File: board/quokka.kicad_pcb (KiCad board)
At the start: 4 copper layers, 228.6 x 184.1 mm, 337 parts, among them J1301 FPGA JTAG, J201 Barrel_Jack, J301 ARM SWD, J302 Conn_01x02, J303 Conn_01x09, J304 Conn_01x03, J305 USB_B, J401 Conn_01x09, Q1201 Q_NPN_BEC, Q1301 Q_NPN_BEC, Q1401 Q_NPN_BEC, Q1402 Q_NPN_BEC, Q1403 Q_NPN_BEC, Q201 Q_PMOS_GSD, Q601 Q_PMOS_GSD, Q602 Q_PMOS_GSD, Q603 Q_PMOS_GSD, Q604 Q_PMOS_GSD, Q605 Q_PMOS_GSD, Q606 Q_PMOS_GSD, Q607 Q_PMOS_GSD, Q608 Q_PMOS_GSD, Q701 Q_PMOS_GSD, Q702 Q_PMOS_GSD, Q703 Q_PMOS_GSD, Q704 Q_PMOS_GSD, Q705 Q_PMOS_GSD, Q706 Q_PMOS_GSD, Q707 Q_PMOS_GSD, Q708 Q_PMOS_GSD, Q801 Q_PMOS_GSD, Q802 Q_PMOS_GSD, Q803 Q_PMOS_GSD, Q804 Q_PMOS_GSD, Q805 Q_PMOS_GSD, Q806 Q_PMOS_GSD, Q807 Q_PMOS_GSD, SW901 SW_SPST, SW902 SW_SPST, SW903 SW_SPST, SW904 SW_SPST, SW905 SW_SPST, SW906 SW_SPST, SW907 SW_SPST, SW908 SW_SPST, SW909 SW_SPST, SW910 SW_SPST, SW911 SW_SPST, SW912 SW_SPST, SW913 SW_SPST, SW914 SW_SPST, SW915 SW_SPST, SW916 SW_SPST, SW917 SW_SPST, SW918 SW_SPST, SW919 SW_SPST, SW920 SW_SPST, SW921 SW_SPST, SW922 SW_SPST, SW923 SW_SPST, SW924 SW_SPST, SW925 SW_SPST, SW926 SW_SPST, SW927 SW_SPST, SW928 SW_SPST, SW929 SW_SPST, SW930 SW_SPST, U1001 DIN96, U1101 AS6C8008, U1201 74HCT245, U1202 6502, U1203 74HCT245, U1204 74HCT245, U1205 74HCT245, U1401 74LVC4245A, U1402 74LVC4245A, U1403 74LVC4245A, U1404 74LVC4245A, U1405 74LVC4245A, U1406 74LVC4245A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

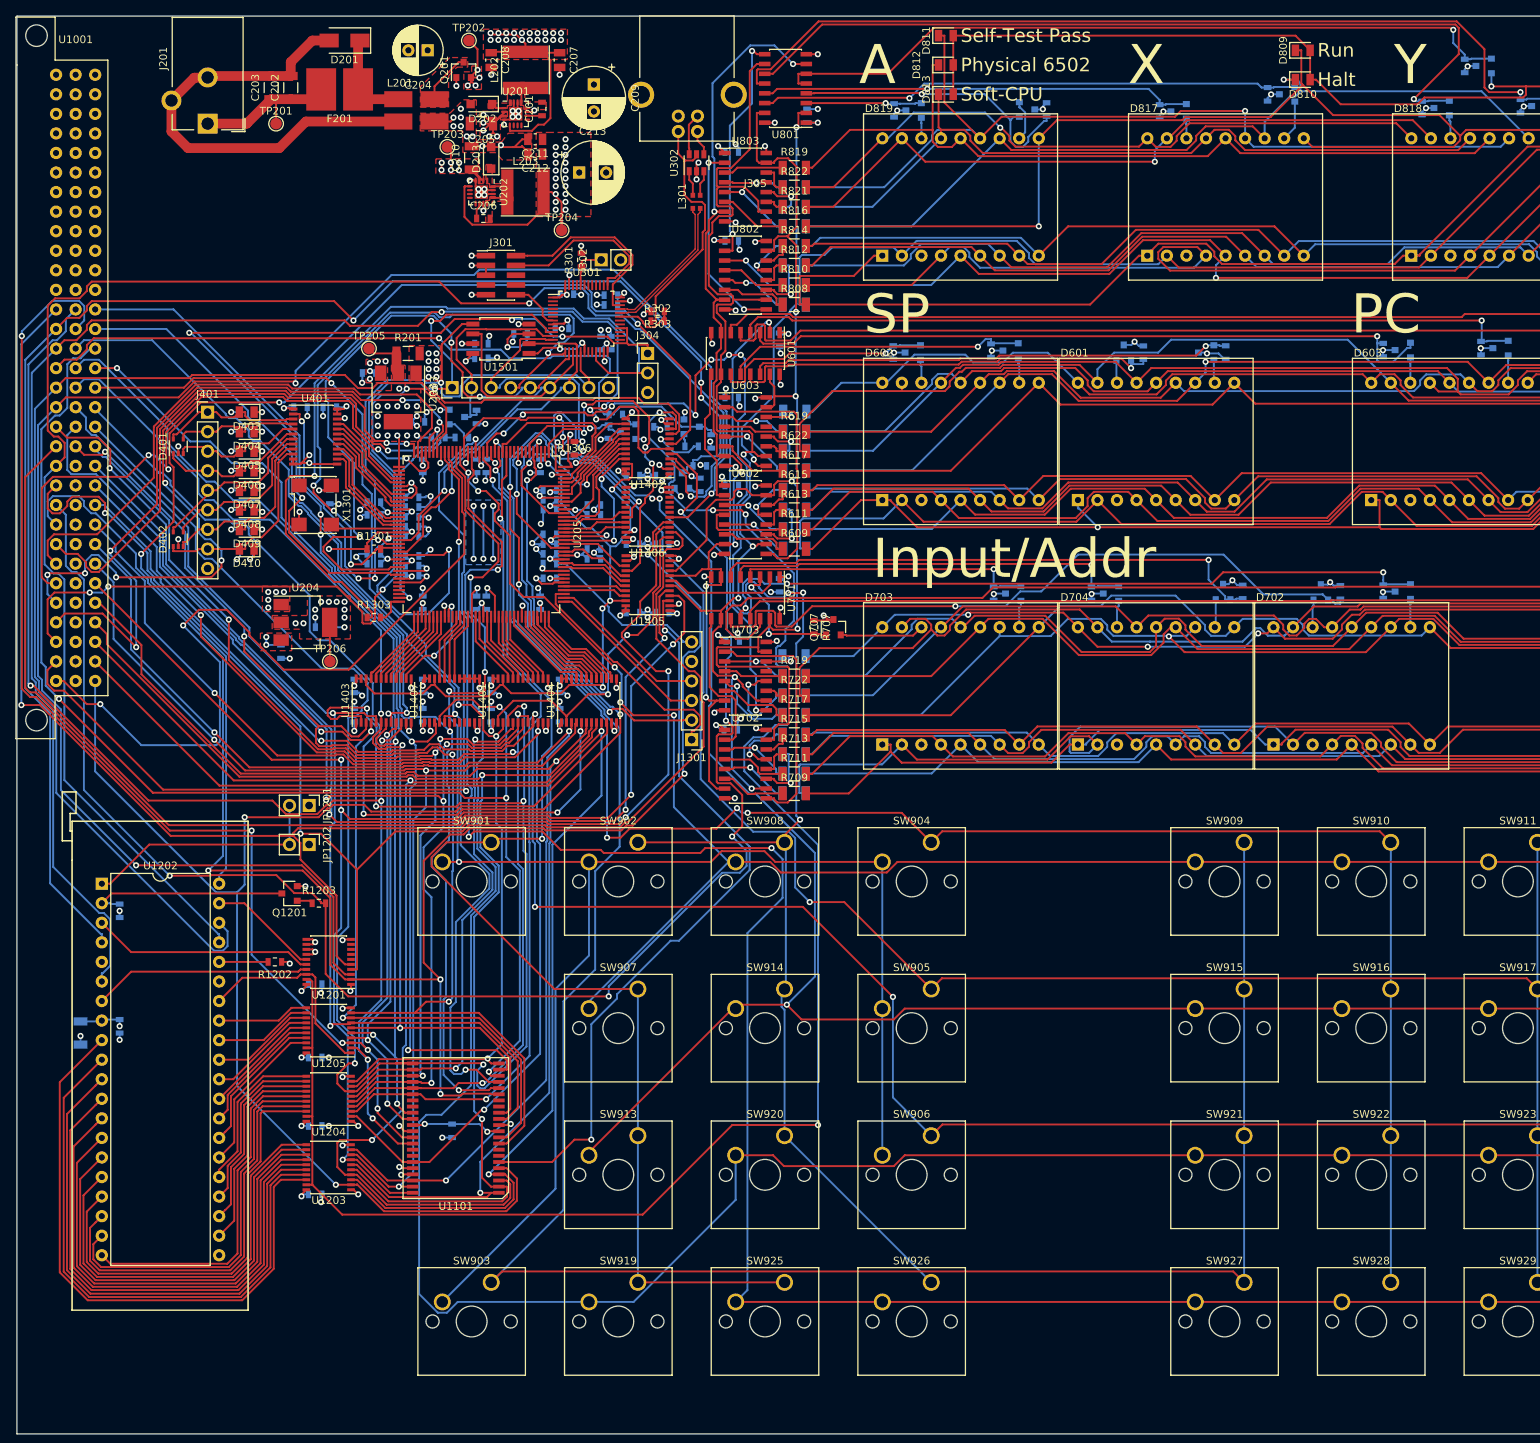
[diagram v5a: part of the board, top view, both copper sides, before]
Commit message: Cleaned up DRC violations
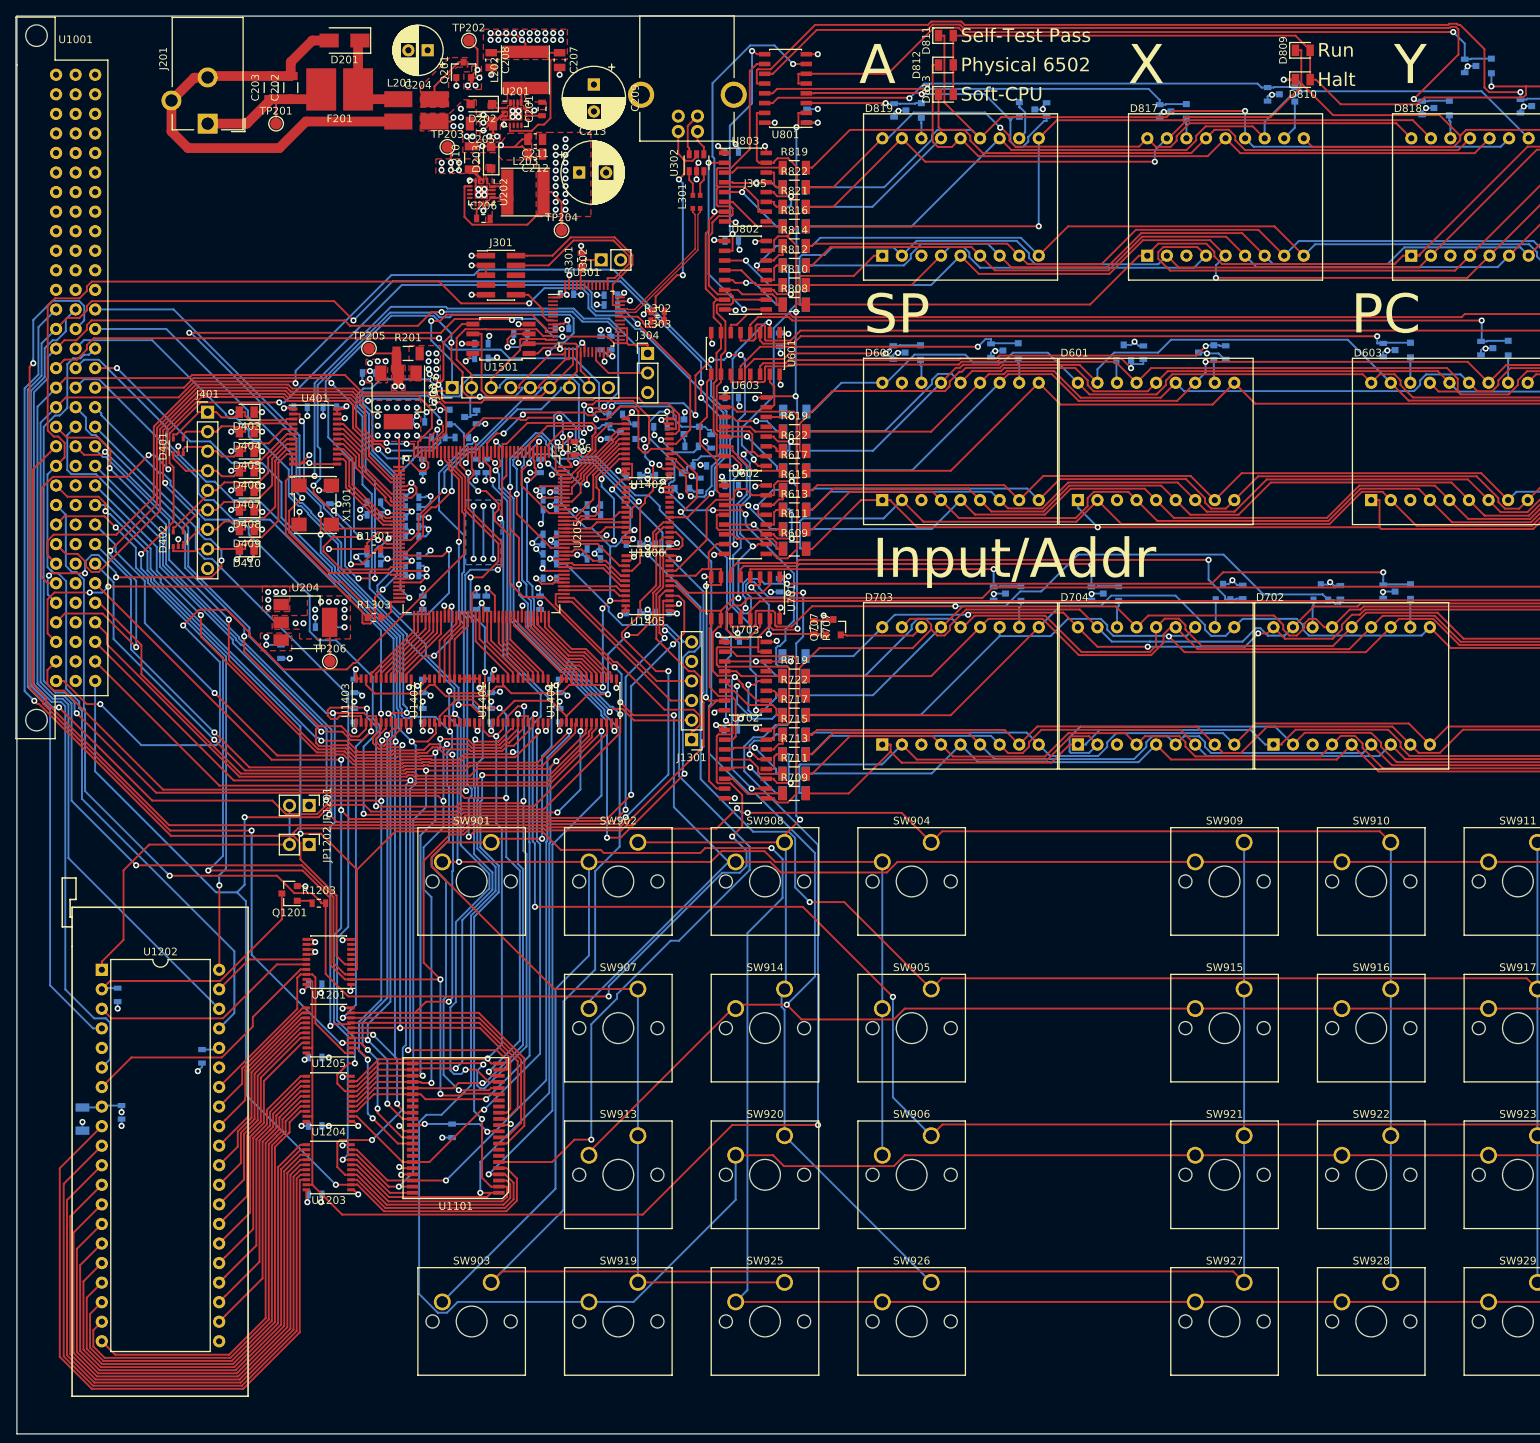
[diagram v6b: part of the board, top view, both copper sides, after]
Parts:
- R1202: moved to B.Cu
- moved R1202 15.5 mm to (184.7, 170.0), turned to 90 degrees
- moved C1202 11.2 mm to (174.2, 177.3)
- moved C1203 11.2 mm to (169.2, 178.2)
- moved U1202 11.2 mm to (171.7, 158.8)
- moved R1201 10.9 mm to (173.7, 162.1)
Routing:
- net /6502/6502_PHI0: track 213.3 -> 225.8 mm
- net /6502/6502_~NMI: track 195.2 -> 207.4 mm
- net /6502/6502_~IRQ: track 198.5 -> 210.0 mm
- net /6502/6502_~RES: track 157.4 -> 168.6 mm, vias 3 -> 4
- net /6502/A7: track 55.3 -> 66.0 mm
- net /6502/A6: track 58.7 -> 69.2 mm
- net Net-(JP1201-Pad2): track 31.6 -> 42.1 mm
- net /6502/A5: track 62.0 -> 72.5 mm
- net /6502/A4: track 65.3 -> 75.7 mm
- net /6502/D4: track 15.1 -> 25.5 mm
- net /6502/D5: track 17.1 -> 27.4 mm
- net /6502/A3: track 68.6 -> 79.0 mm
- net /6502/D6: track 19.0 -> 29.3 mm
- net /6502/D7: track 20.8 -> 31.1 mm
- net /6502/A2: track 72.0 -> 82.2 mm
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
